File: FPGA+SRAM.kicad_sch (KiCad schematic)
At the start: 0 parts

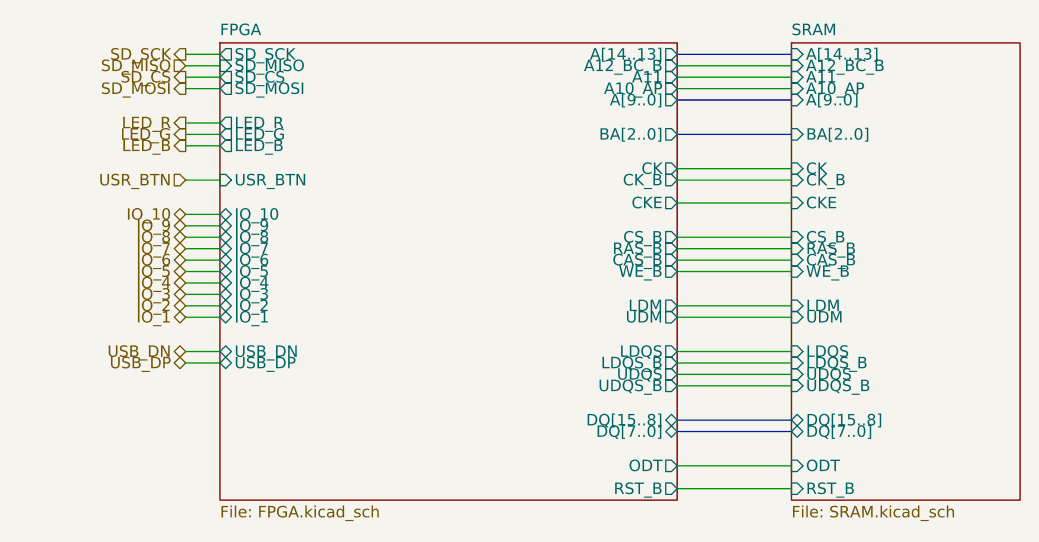
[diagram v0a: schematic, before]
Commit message: Added more I/O. Changed power regulators
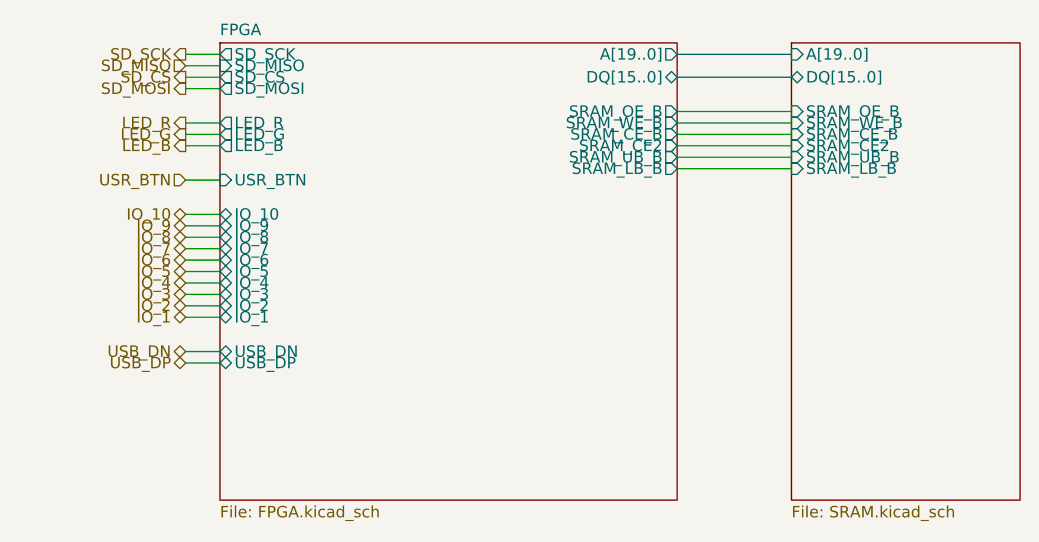
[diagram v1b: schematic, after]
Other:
- sheet FPGA ports: added A[19..0], DQ[15..0], SRAM_CE2, SRAM_CE_B, SRAM_LB_B, SRAM_OE_B, SRAM_UB_B, SRAM_WE_B; removed A10_AP, A11, A12_BC_B, A[14..13], A[9..0], BA[2..0], CAS_B, CK, CKE, CK_B, CS_B, DQ[15..8], DQ[7..0], LDM, LDQS, LDQS_B, ODT, RAS_B, RST_B, UDM, UDQS, UDQS_B, WE_B
- sheet SRAM ports: added A[19..0], DQ[15..0], SRAM_CE2, SRAM_CE_B, SRAM_LB_B, SRAM_OE_B, SRAM_UB_B, SRAM_WE_B; removed A10_AP, A11, A12_BC_B, A[14..13], A[9..0], BA[2..0], CAS_B, CK, CKE, CK_B, CS_B, DQ[15..8], DQ[7..0], LDM, LDQS, LDQS_B, ODT, RAS_B, RST_B, UDM, UDQS, UDQS_B, WE_B

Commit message: Power routed. Saving before reworking ICE40 pins to optimize layout
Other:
- sheet FPGA ports: added CDONE, FIFO[7..0], FIFO_RD_B, FIFO_RXF_B, FIFO_TXE_B, FIFO_WR_B, IO_B[10..1], IO_T[10..1], SD_CLK, SD_CMD, SD_DAT[3..0], SPI_CNFG_CS_B, SPI_CNFG_DI, SPI_CNFG_DO, SPI_CNFG_SCK, USB2_DN, USB2_DP, USB3_DN, USB3_DP, USR_BTN1; removed IO_1, IO_10, IO_2, IO_3, IO_4, IO_5, IO_6, IO_7, IO_8, IO_9, SD_CS, SD_MISO, SD_MOSI, SD_SCK, USB_DN, USB_DP, USR_BTN
